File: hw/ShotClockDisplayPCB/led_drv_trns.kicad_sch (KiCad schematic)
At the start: 9 parts, among them Q1 Q_NPN_BCE, Q1 Q_PMOS_SGD

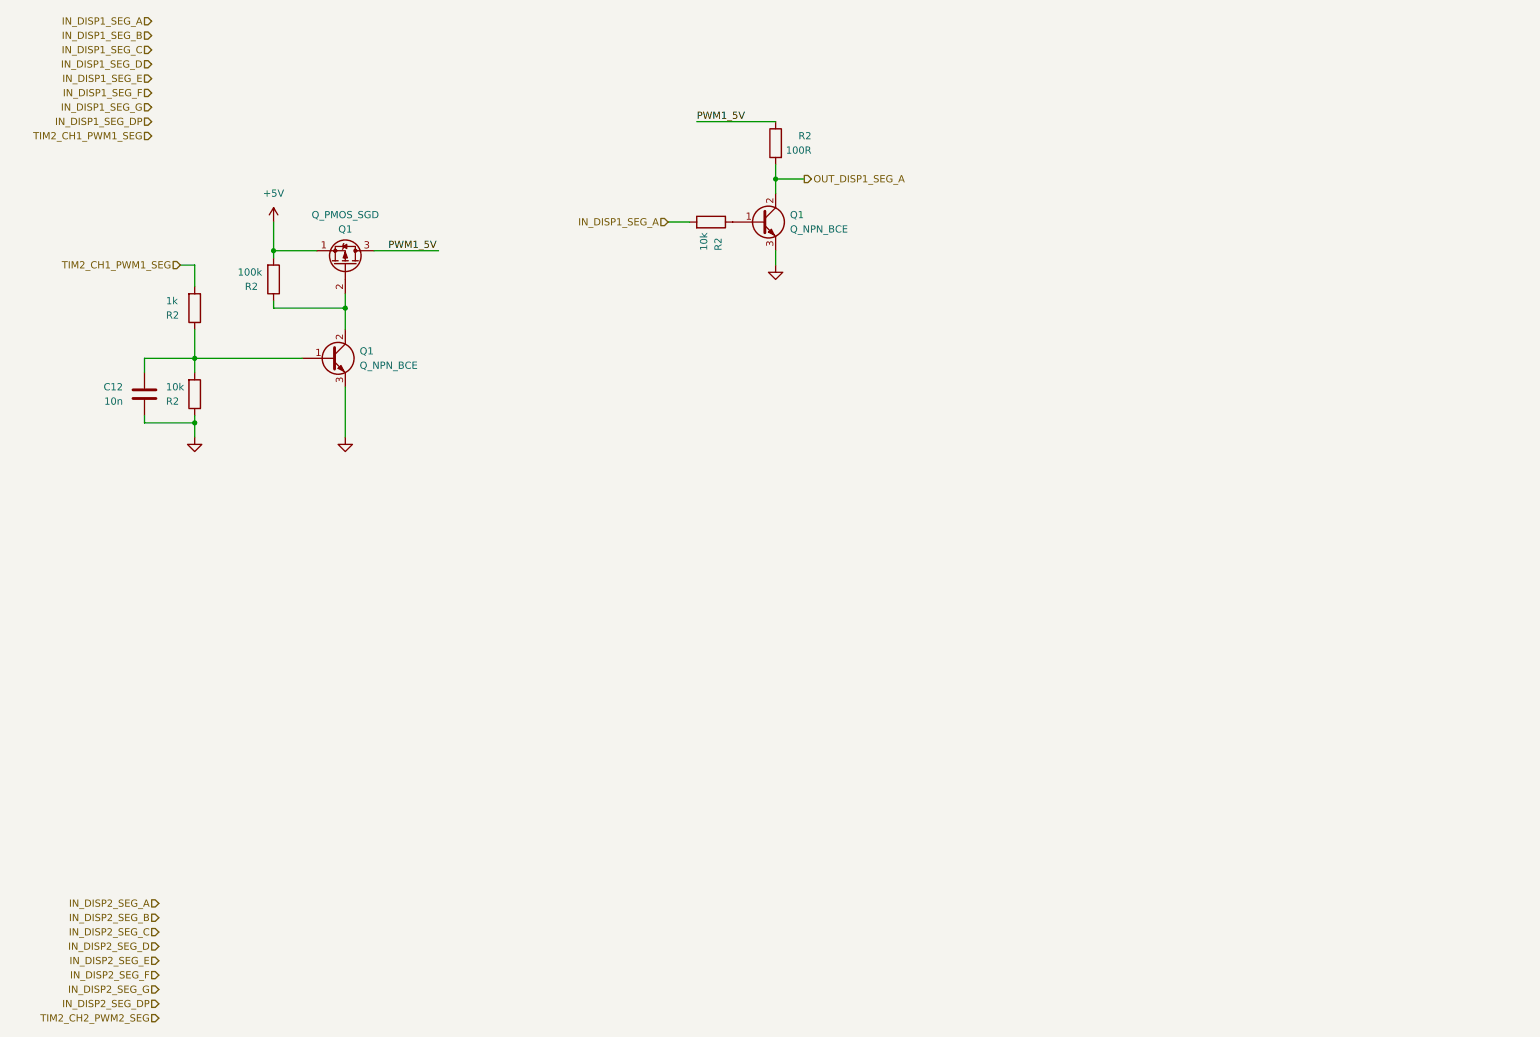
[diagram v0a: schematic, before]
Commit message: Finshed both schematics
- LED driving transistors are placed
- All connectors on segment display PCB are placed
- All schematic references have been re-configured (autosort on Y axis)
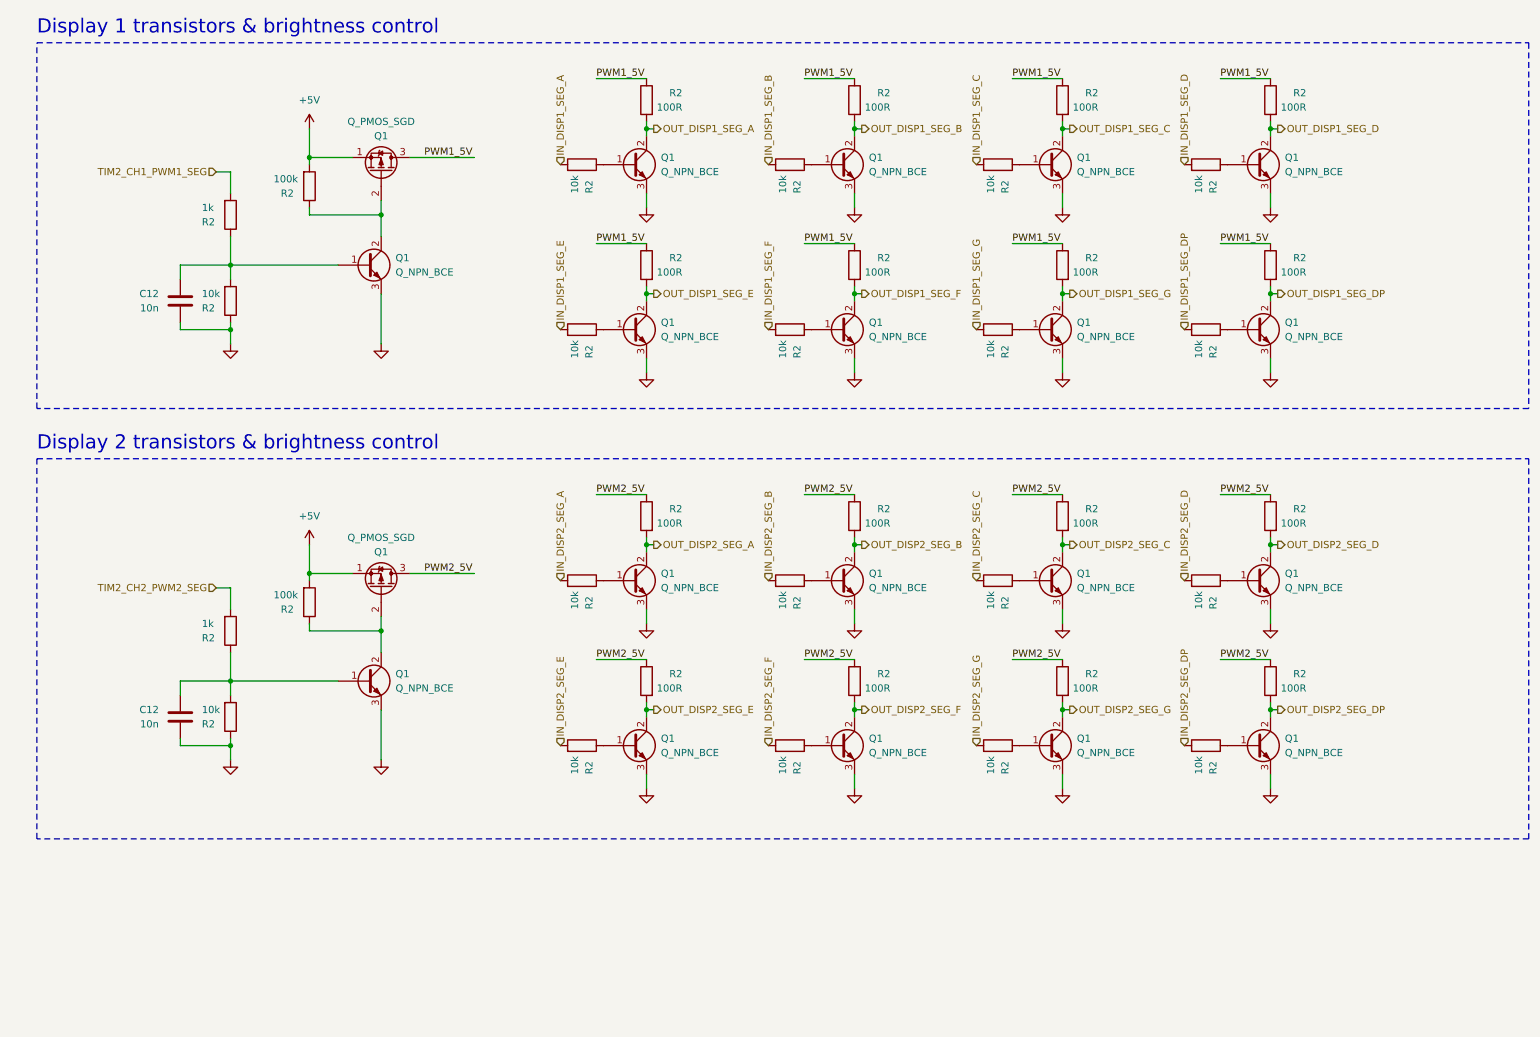
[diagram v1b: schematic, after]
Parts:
- added C12: 10n, Capacitor_SMD:C_0603_1608Metric, symbol Device:C
- added Q1: Q_PMOS_SGD, Package_TO_SOT_SMD:SOT-23, symbol Device:Q_PMOS_SGD
- added Q1 (x16): Q_NPN_BCE, Package_TO_SOT_SMD:SOT-23, symbol Device:Q_NPN_BCE
- added R2 (x15): 100R, Resistor_SMD:R_0402_1005Metric, symbol Device:R
- added R2 (x16): 10k, Resistor_SMD:R_0402_1005Metric, symbol Device:R
- added R2: 100k, Resistor_SMD:R_0402_1005Metric, symbol Device:R
- added R2: 1k, Resistor_SMD:R_0402_1005Metric, symbol Device:R
- Q1: footprint Package_TO_SOT_SMD:SC-59 -> Package_TO_SOT_SMD:SOT-23
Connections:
- net +5V: now also Q1.1 (S), R2.2
- net GND: now also C12.2, Q1.3 (E), Q1.3 (E), Q1.3 (E), Q1.3 (E), Q1.3 (E), Q1.3 (E), Q1.3 (E), Q1.3 (E), Q1.3 (E), Q1.3 (E), Q1.3 (E), Q1.3 (E), Q1.3 (E), Q1.3 (E), Q1.3 (E), Q1.3 (E), R2.1
- net IN_DISP1_SEG_B: now also R2.2
- net IN_DISP1_SEG_C: now also R2.2
- net IN_DISP1_SEG_D: now also R2.2
- net IN_DISP1_SEG_DP: now also R2.2
- net IN_DISP1_SEG_E: now also R2.2
- net IN_DISP1_SEG_F: now also R2.2
- net IN_DISP1_SEG_G: now also R2.2
- net IN_DISP2_SEG_A: now also R2.2
- net IN_DISP2_SEG_B: now also R2.2
- net IN_DISP2_SEG_C: now also R2.2
- net IN_DISP2_SEG_D: now also R2.2
- net IN_DISP2_SEG_DP: now also R2.2
- net IN_DISP2_SEG_E: now also R2.2
- net IN_DISP2_SEG_F: now also R2.2
- net IN_DISP2_SEG_G: now also R2.2
- net PWM1_5V: now also R2.1, R2.1, R2.1, R2.1, R2.1, R2.1, R2.1
- net TIM2_CH2_PWM2_SEG: now also R2.2
- new net: Q1.2 (C), Q1.2 (G), R2.1
- new net: Q1.1 (B), R2.1 (x15)
- new net: C12.1, Q1.1 (B), R2.1, R2.2
- new net OUT_DISP1_SEG_B: Q1.2 (C), R2.2
- new net OUT_DISP1_SEG_C: Q1.2 (C), R2.2
- new net OUT_DISP1_SEG_D: Q1.2 (C), R2.2
- new net OUT_DISP1_SEG_DP: Q1.2 (C), R2.2
- new net OUT_DISP1_SEG_E: Q1.2 (C), R2.2
- new net OUT_DISP1_SEG_F: Q1.2 (C), R2.2
- new net OUT_DISP1_SEG_G: Q1.2 (C), R2.2
- new net OUT_DISP2_SEG_A: Q1.2 (C), R2.2
- new net OUT_DISP2_SEG_B: Q1.2 (C), R2.2
- new net OUT_DISP2_SEG_C: Q1.2 (C), R2.2
- new net OUT_DISP2_SEG_D: Q1.2 (C), R2.2
- new net OUT_DISP2_SEG_DP: Q1.2 (C), R2.2
- new net OUT_DISP2_SEG_E: Q1.2 (C), R2.2
- new net OUT_DISP2_SEG_F: Q1.2 (C), R2.2
- new net OUT_DISP2_SEG_G: Q1.2 (C), R2.2
- new net PWM2_5V: Q1.3 (D), R2.1, R2.1, R2.1, R2.1, R2.1, R2.1, R2.1, R2.1
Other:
- note added: "Display 1 transistors & brightness control"
- note added: "Display 2 transistors & brightness control"
- moved on the sheet: C12, Q1, R2

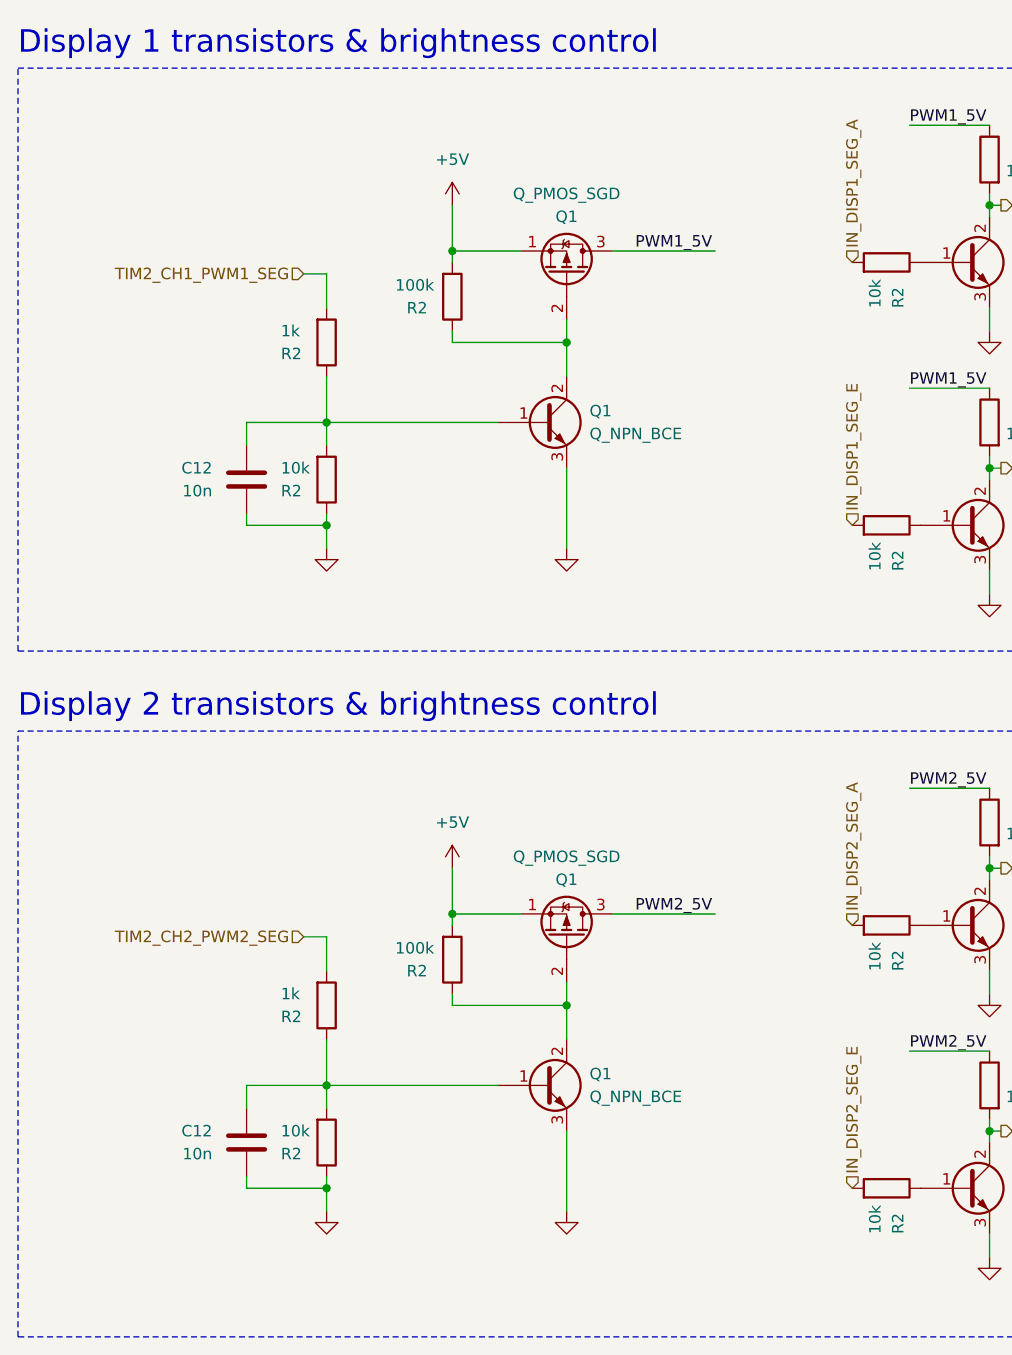
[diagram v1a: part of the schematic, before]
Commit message: Display print
Changed mainboard connector to FPC connector
Created routing for board
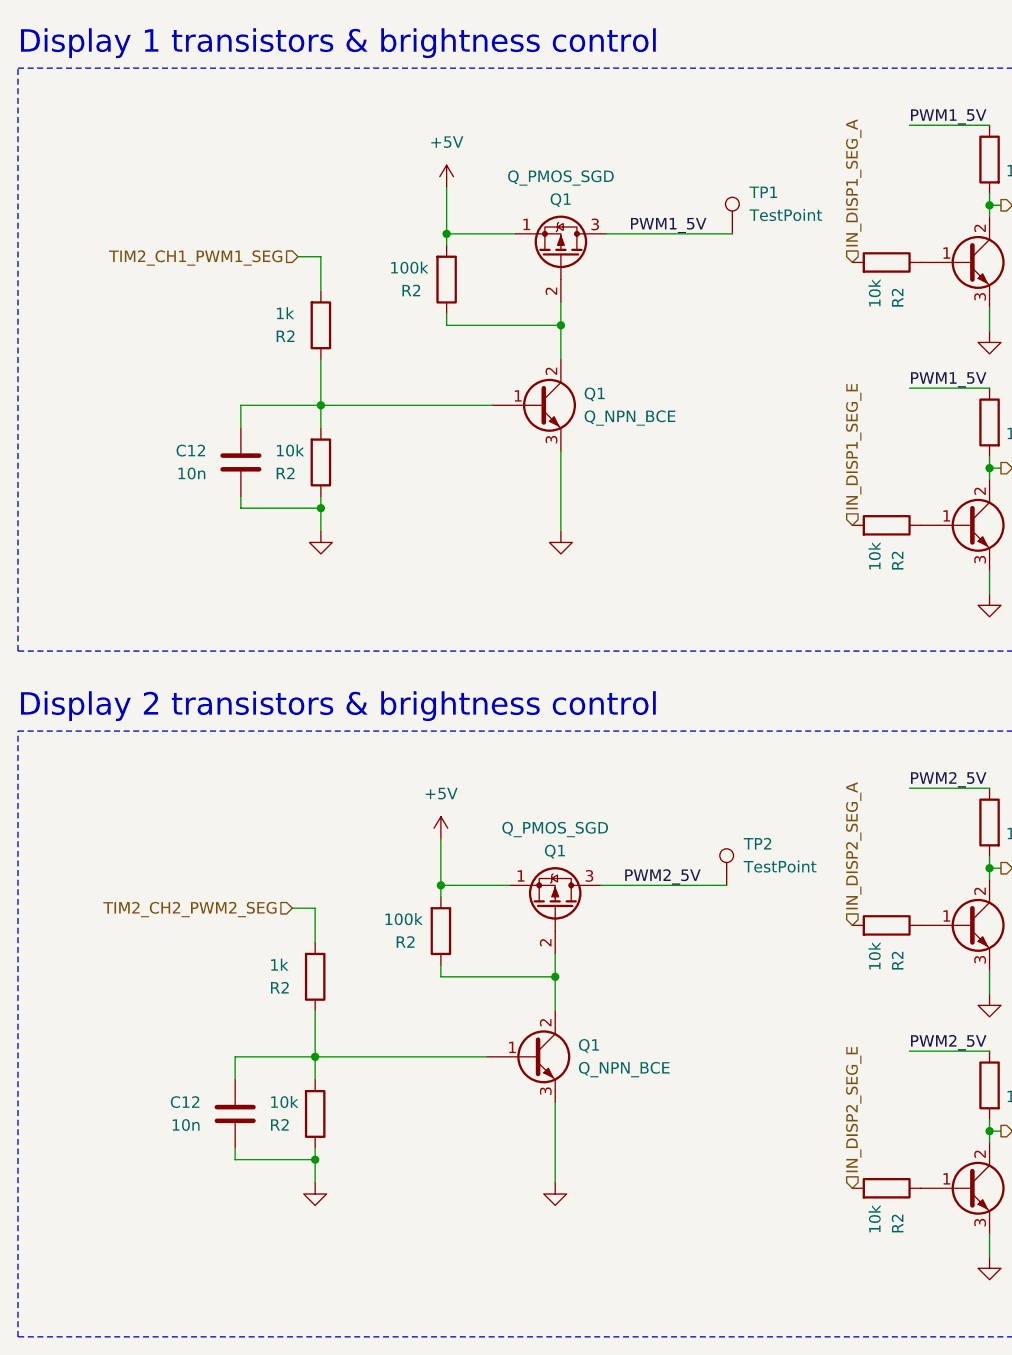
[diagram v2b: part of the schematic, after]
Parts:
- added TP1, TP2: TestPoint, TestPoint:TestPoint_Pad_D1.0mm, symbol Connector:TestPoint
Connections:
- net PWM1_5V: now also TP1.1
- net PWM2_5V: now also TP2.1
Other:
- moved on the sheet: C12, Q1, R2
